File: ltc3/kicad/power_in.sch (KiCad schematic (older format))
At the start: 0 parts

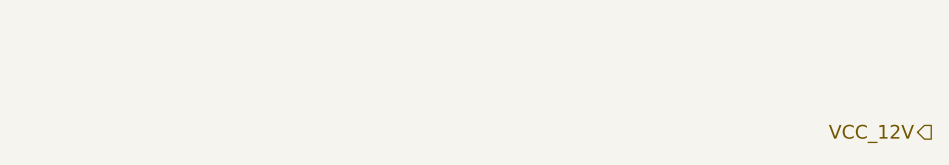
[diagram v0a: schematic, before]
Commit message: Fixed mistakes in triggers schematic; misc. clean-up.
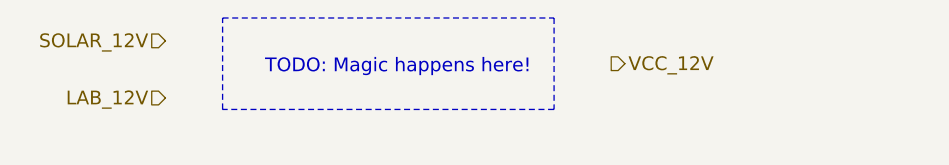
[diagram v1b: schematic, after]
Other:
- note added: "TODO: Magic happens here!"
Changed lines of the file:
@@
 Comment4 ""
 $EndDescr
-Text HLabel 6000 2900 0    60   Output ~ 0
+Text HLabel 4600 2600 2    60   Output ~ 0
 VCC_12V
+Text HLabel 2650 2500 0    60   Input ~ 0
+SOLAR_12V
+Text HLabel 2650 2750 0    60   Input ~ 0
+LAB_12V
+Text Notes 4250 2650 2    60   ~ 0
+TODO: Magic happens here!
+Wire Notes Line
+	2900 2400 4350 2400
+Wire Notes Line
+	4350 2400 4350 2800
+Wire Notes Line
+	4350 2800 2900 2800
+Wire Notes Line
+	2900 2800 2900 2400
 $EndSCHEMATC

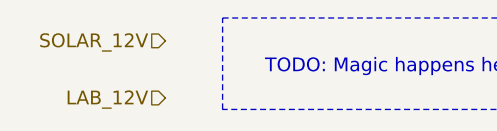
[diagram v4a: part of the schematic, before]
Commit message: Modified LTC3 external device support schematics. 1. Split single sheet into separate power and trigger sheets. 2. Added current-limiting resistor to LED input pin on each    photorelay. 3. Added bleed resistor and filter capacitor across each output    connector.
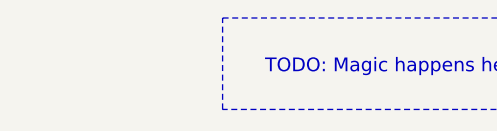
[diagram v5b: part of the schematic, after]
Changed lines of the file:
@@
 $Descr B 17000 11000
 encoding utf-8
-Sheet 2 6
+Sheet 2 7
 Title "LTC3 Power Inputs (Solar, Lab)"
-Date "8 apr 2015"
+Date "18 apr 2015"
 Rev "1"
 Comp "Portland State Aerospace Society <http://psas.pdx.edu/>"
@@
 Text HLabel 4600 2600 2    60   Output ~ 0
 VCC_12V
-Text HLabel 2650 2500 0    60   Input ~ 0
-SOLAR_12V
-Text HLabel 2650 2750 0    60   Input ~ 0
-LAB_12V
 Text Notes 4250 2650 2    60   ~ 0
 TODO: Magic happens here!

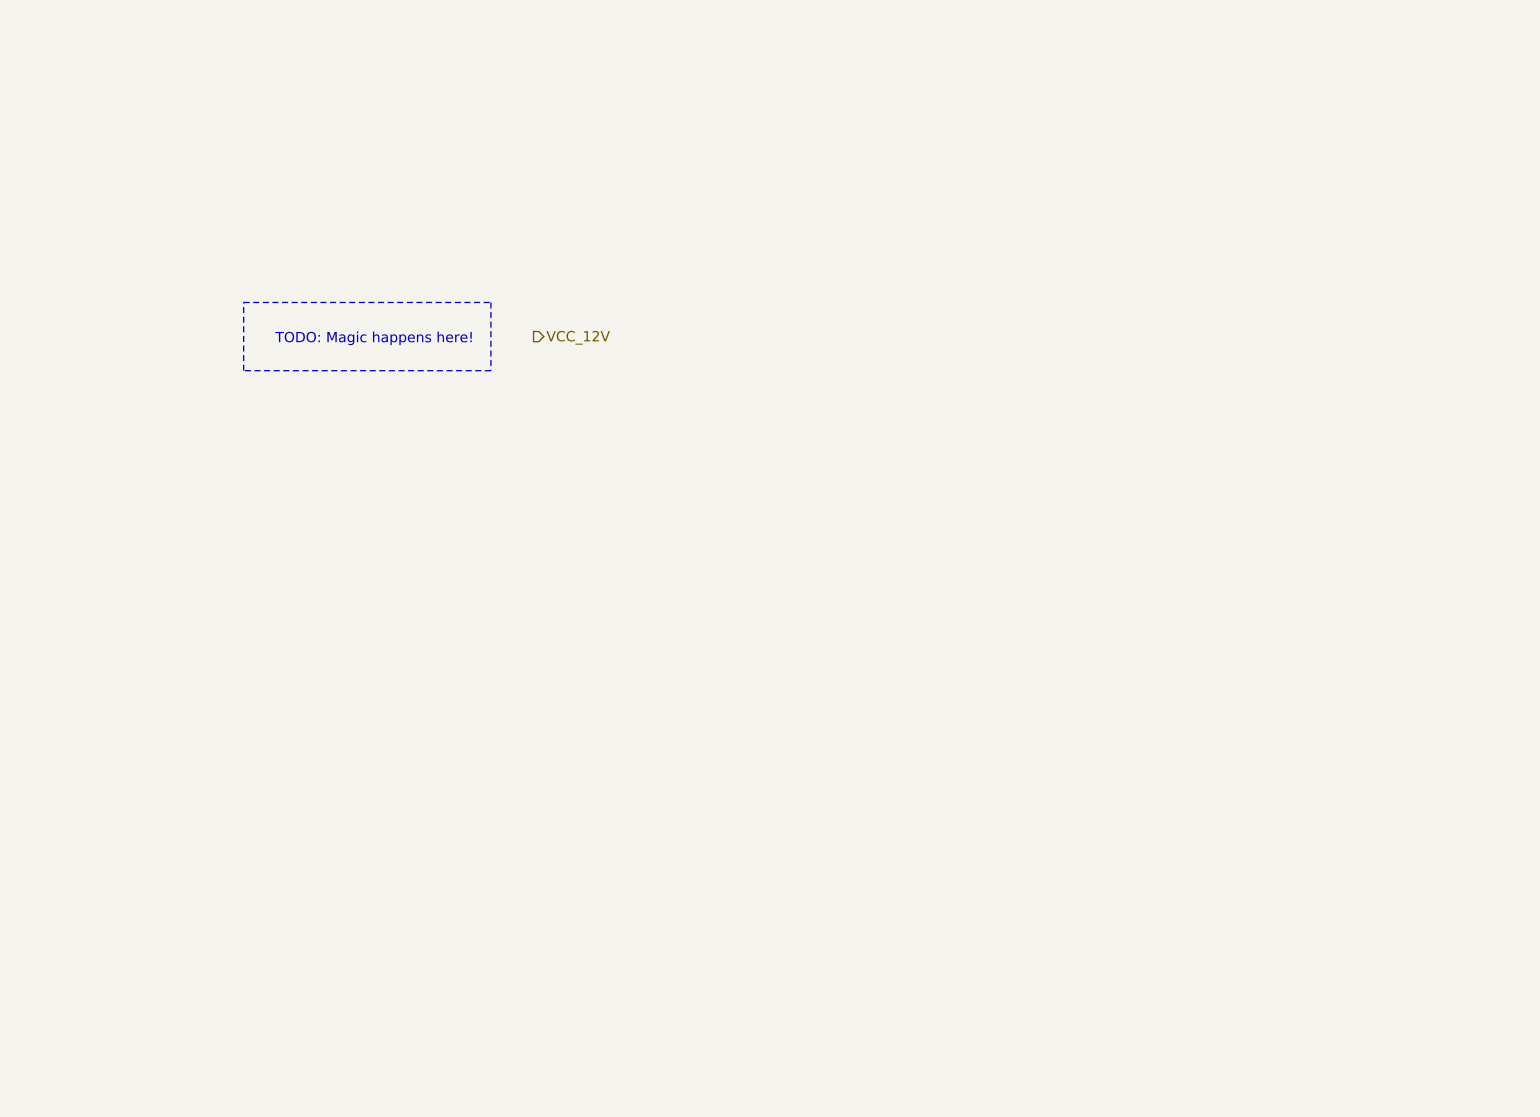
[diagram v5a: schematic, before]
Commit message: LTC3 KiCad updates. 1. Modified schematics to play nicely with (relatively) recent changes    in KiCad's stock component libraries (e.g., redrawn capacitor and    resistor symbols). 2. Began work on PTN78020-based DC-DC converter schematics.
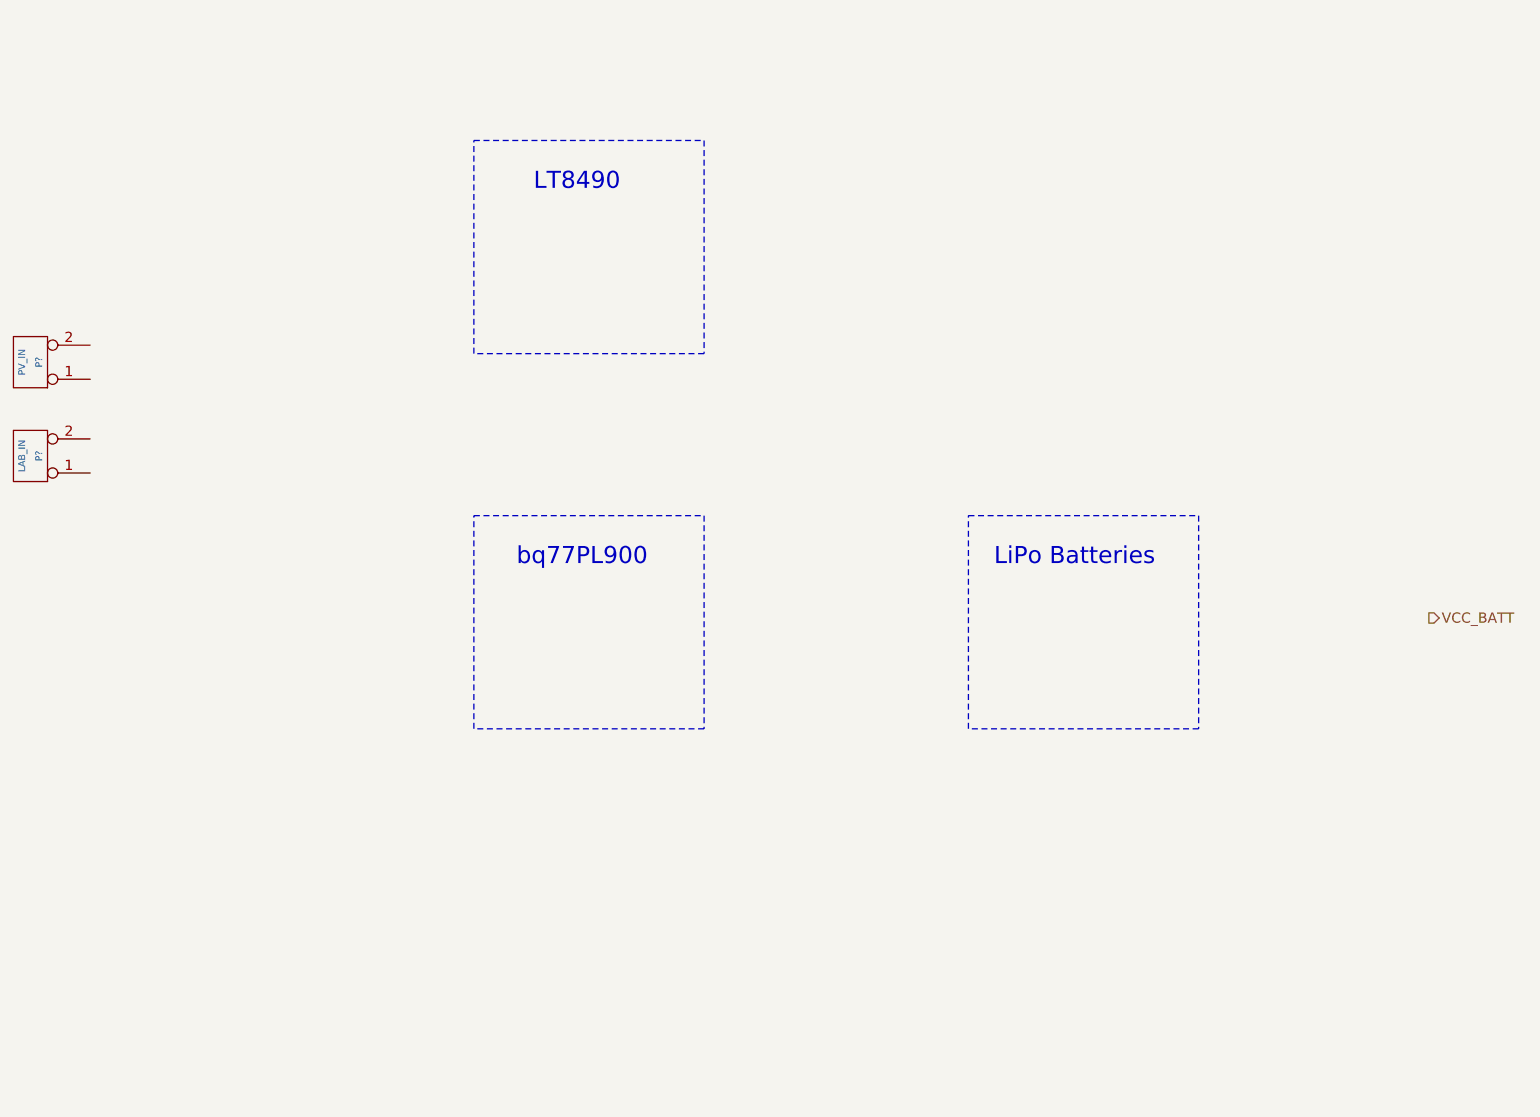
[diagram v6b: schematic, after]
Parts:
- added P?: PV_IN, symbol CONN_2
- added P?: LAB_IN, symbol CONN_2
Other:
- note added: "LT8490"
- note added: "LiPo Batteries"
- note added: "bq77PL900"
- note removed: "TODO: Magic happens here!"
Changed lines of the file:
@@
 LIBS:memory
 LIBS:xilinx
-LIBS:special
 LIBS:microcontrollers
 LIBS:dsp
@@
 LIBS:switches
 LIBS:Toshiba
+LIBS:LTC3_components
 LIBS:Launch_Tower_Computer_III-cache
-EELAYER 27 0
+EELAYER 25 0
 EELAYER END
 $Descr B 17000 11000
@@
 Sheet 2 7
 Title "LTC3 Power Inputs (Solar, Lab)"
-Date "18 apr 2015"
+Date "16 may 2015"
 Rev "1"
 Comp "Portland State Aerospace Society <http://psas.pdx.edu/>"
@@
 Comment4 ""
 $EndDescr
-Text HLabel 4600 2600 2    60   Output ~ 0
-VCC_12V
-Text Notes 4250 2650 2    60   ~ 0
-TODO: Magic happens here!
+Text HLabel 9850 4250 2    60   Output ~ 0
+VCC_BATT
+$Comp
+L CONN_2 P?
+U 1 1 5557CEAC
+P 1650 2750
+F 0 "P?" V 1600 2750 40  0000 C CNN
+F 1 "PV_IN" V 1700 2750 40  0000 C CNN
+F 2 "" H 1650 2750 60  0000 C CNN
+F 3 "" H 1650 2750 60  0000 C CNN
+	1    1650 2750
+	-1   0    0    1
+$EndComp
+$Comp
+L CONN_2 P?
+U 1 1 5557CEBB
+P 1650 3300
+F 0 "P?" V 1600 3300 40  0000 C CNN
+F 1 "LAB_IN" V 1700 3300 40  0000 C CNN
+F 2 "" H 1650 3300 60  0000 C CNN
+F 3 "" H 1650 3300 60  0000 C CNN
+	1    1650 3300
+	-1   0    0    1
+$EndComp
 Wire Notes Line
-	2900 2400 4350 2400
+	4250 1450 5600 1450
 Wire Notes Line
-	4350 2400 4350 2800
+	5600 1450 5600 2700
 Wire Notes Line
-	4350 2800 2900 2800
+	5600 2700 4250 2700
 Wire Notes Line
-	2900 2800 2900 2400
+	4250 2700 4250 1450
+Text Notes 4600 1750 0    100  ~ 0
+LT8490
+Wire Notes Line
+	4250 3650 5600 3650
+Wire Notes Line
+	5600 3650 5600 4900
+Wire Notes Line
+	5600 4900 4250 4900
+Wire Notes Line
+	4250 4900 4250 3650
+Text Notes 4500 3950 0    100  ~ 0
+bq77PL900
+Wire Notes Line
+	7150 3650 8500 3650
+Wire Notes Line
+	8500 3650 8500 4900
+Wire Notes Line
+	8500 4900 7150 4900
+Wire Notes Line
+	7150 4900 7150 3650
+Text Notes 7300 3950 0    100  ~ 0
+LiPo Batteries
 $EndSCHEMATC

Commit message: Added lt8490 schematic and footprint to libs.
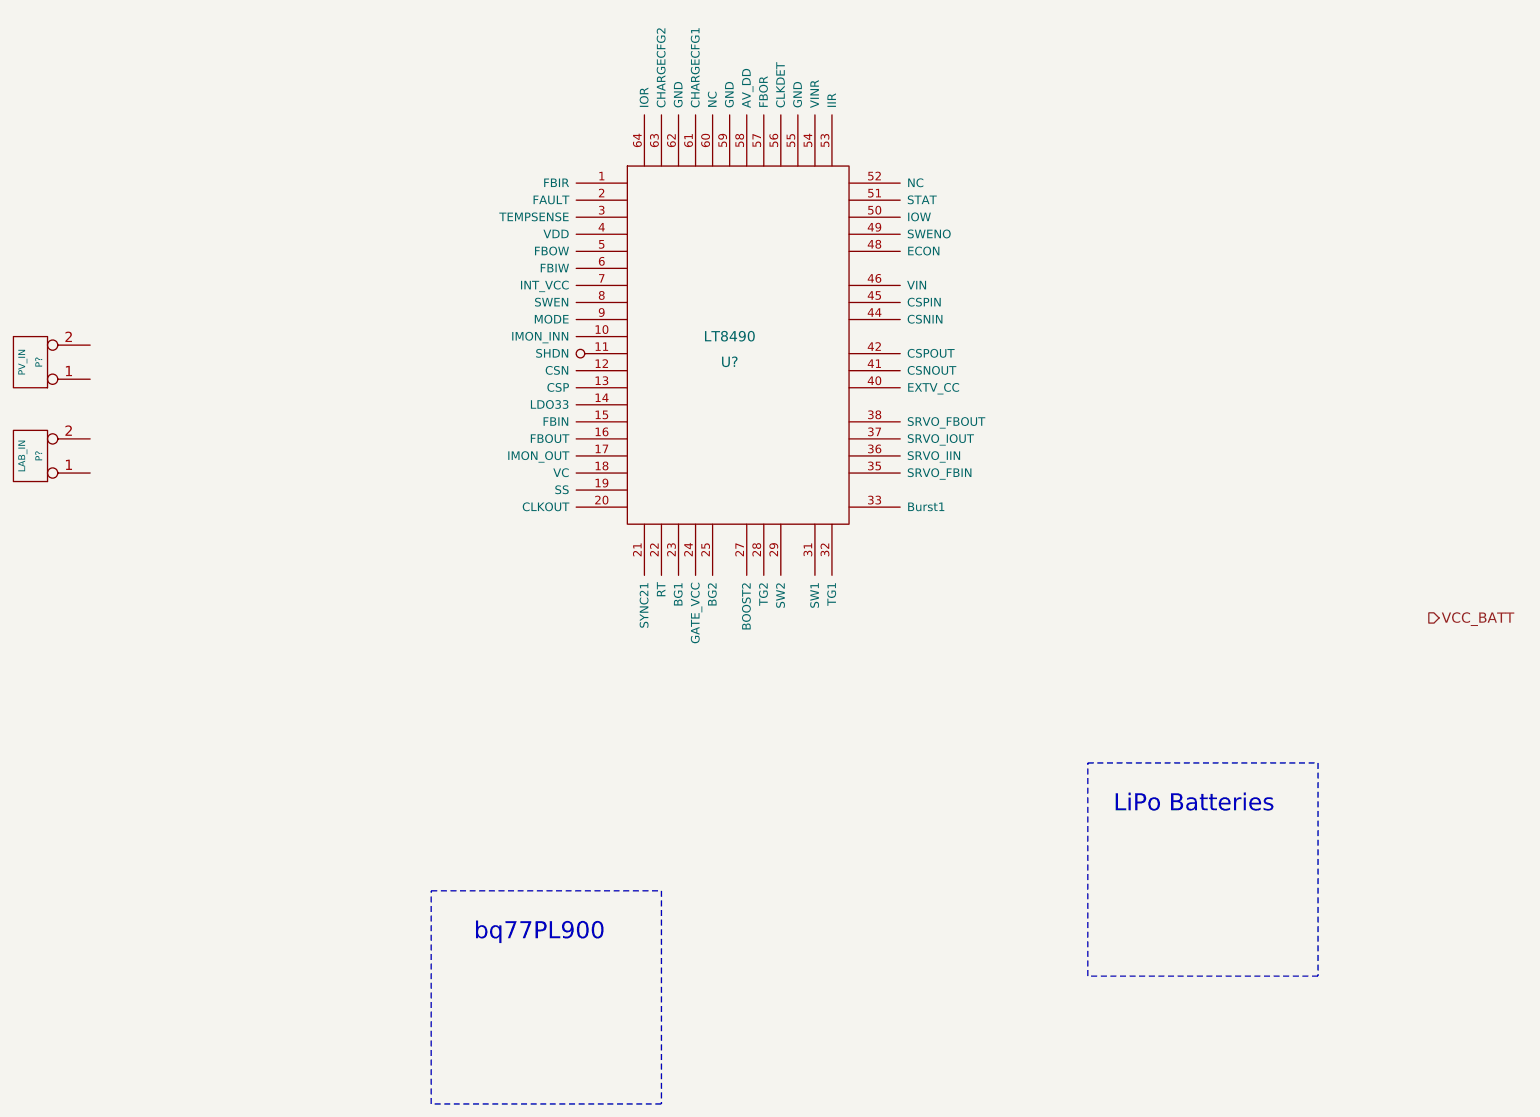
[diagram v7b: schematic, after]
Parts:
- added U?: LT8490, ~, symbol LT8490
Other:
- note removed: "LT8490"
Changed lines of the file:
@@
 LIBS:memory
 LIBS:xilinx
+LIBS:special
 LIBS:microcontrollers
 LIBS:dsp
@@
 LIBS:contrib
 LIBS:valves
-LIBS:headers
-LIBS:DIP_switches
-LIBS:LTC299x
-LIBS:memory_devices
-LIBS:switches
-LIBS:Toshiba
 LIBS:LTC3_components
 LIBS:Launch_Tower_Computer_III-cache
-EELAYER 25 0
+EELAYER 27 0
 EELAYER END
 $Descr B 17000 11000
@@
 Sheet 2 7
 Title "LTC3 Power Inputs (Solar, Lab)"
-Date "16 may 2015"
+Date "23 may 2015"
 Rev "1"
 Comp "Portland State Aerospace Society <http://psas.pdx.edu/>"
@@
 $EndComp
 Wire Notes Line
-	4250 1450 5600 1450
+	4000 5850 5350 5850
 Wire Notes Line
-	5600 1450 5600 2700
+	5350 5850 5350 7100
 Wire Notes Line
-	5600 2700 4250 2700
+	5350 7100 4000 7100
 Wire Notes Line
-	4250 2700 4250 1450
-Text Notes 4600 1750 0    100  ~ 0
-LT8490
-Wire Notes Line
-	4250 3650 5600 3650
-Wire Notes Line
-	5600 3650 5600 4900
-Wire Notes Line
-	5600 4900 4250 4900
-Wire Notes Line
-	4250 4900 4250 3650
-Text Notes 4500 3950 0    100  ~ 0
+	4000 7100 4000 5850
+Text Notes 4250 6150 0    100  ~ 0
 bq77PL900
 Wire Notes Line
-	7150 3650 8500 3650
+	7850 5100 9200 5100
 Wire Notes Line
-	8500 3650 8500 4900
+	9200 5100 9200 6350
 Wire Notes Line
-	8500 4900 7150 4900
+	9200 6350 7850 6350
 Wire Notes Line
-	7150 4900 7150 3650
-Text Notes 7300 3950 0    100  ~ 0
+	7850 6350 7850 5100
+Text Notes 8000 5400 0    100  ~ 0
 LiPo Batteries
+$Comp
+L LT8490 U?
+U 1 1 5560E702
+P 5750 2650
+F 0 "U?" H 5750 2550 60  0000 C CNN
+F 1 "LT8490" H 5750 2700 60  0000 C CNN
+F 2 "~" H 5800 2750 60  0000 C CNN
+F 3 "" H 5800 2750 60  0000 C CNN
+	1    5750 2650
+	1    0    0    -1
+$EndComp
 $EndSCHEMATC

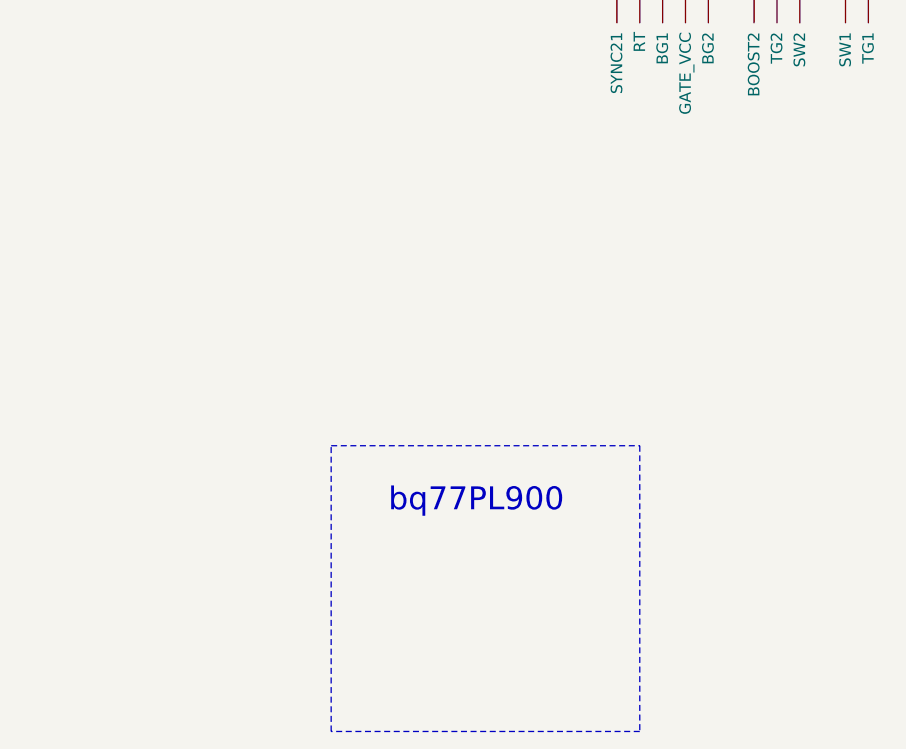
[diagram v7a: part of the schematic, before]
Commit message: Added BQ77PL9000 schematic and footprint to libs.
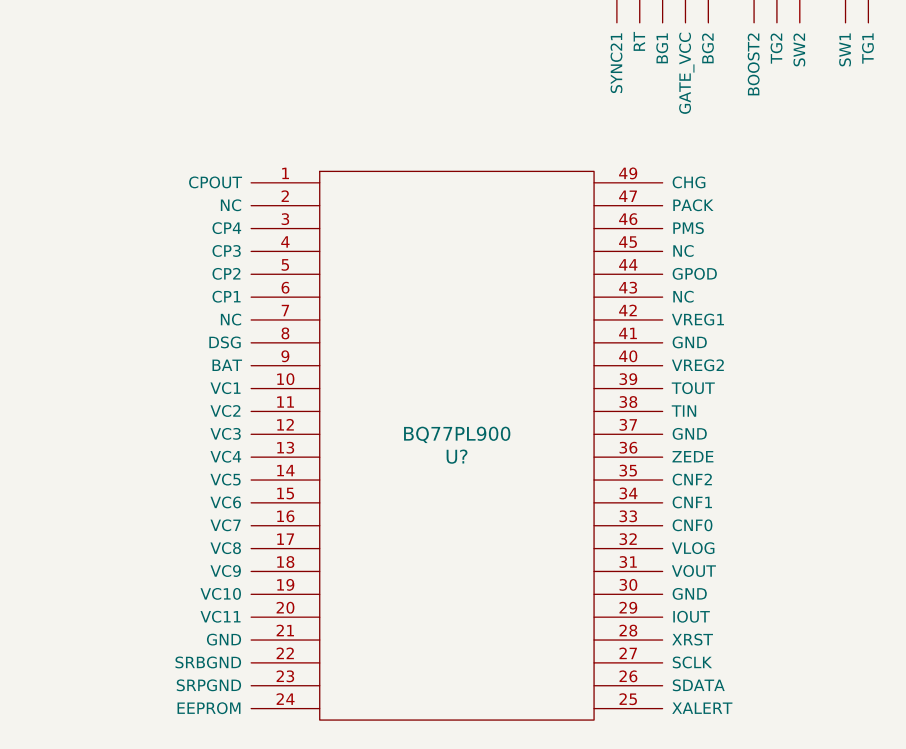
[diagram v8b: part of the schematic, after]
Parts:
- added U?: BQ77PL900, symbol BQ77PL900
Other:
- note removed: "bq77PL900"
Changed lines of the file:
@@
 Sheet 2 7
 Title "LTC3 Power Inputs (Solar, Lab)"
-Date "23 may 2015"
+Date "30 may 2015"
 Rev "1"
 Comp "Portland State Aerospace Society <http://psas.pdx.edu/>"
@@
 $EndComp
 Wire Notes Line
-	4000 5850 5350 5850
-Wire Notes Line
-	5350 5850 5350 7100
-Wire Notes Line
-	5350 7100 4000 7100
-Wire Notes Line
-	4000 7100 4000 5850
-Text Notes 4250 6150 0    100  ~ 0
-bq77PL900
-Wire Notes Line
 	7850 5100 9200 5100
 Wire Notes Line
@@
 	1    0    0    -1
 $EndComp
+$Comp
+L BQ77PL900 U?
+U 1 1 556A16F5
+P 4550 5850
+F 0 "U?" H 4550 5800 60  0000 C CNN
+F 1 "BQ77PL900" H 4550 5900 60  0000 C CNN
+F 2 "" H 4550 5850 60  0000 C CNN
+F 3 "" H 4550 5850 60  0000 C CNN
+	1    4550 5850
+	1    0    0    -1
+$EndComp
